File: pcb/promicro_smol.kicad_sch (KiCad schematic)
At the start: 31 parts, among them Q1 HL3134KT, Q2 HL3134KT, Q3 HL3134KT, Q4 HL3134KT, Q5 HL3134KT, U1 LSM6DSVTR, U2 QMC6309, U4 ProMicro NRF52840

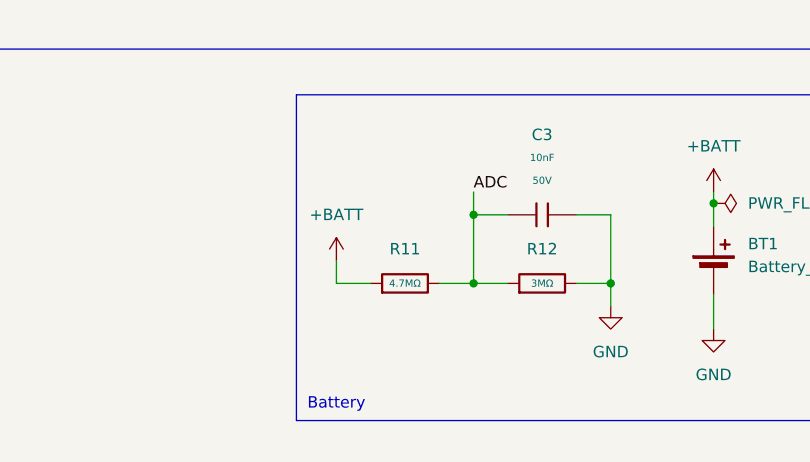
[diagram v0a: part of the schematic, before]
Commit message: feat: routing + ADC res
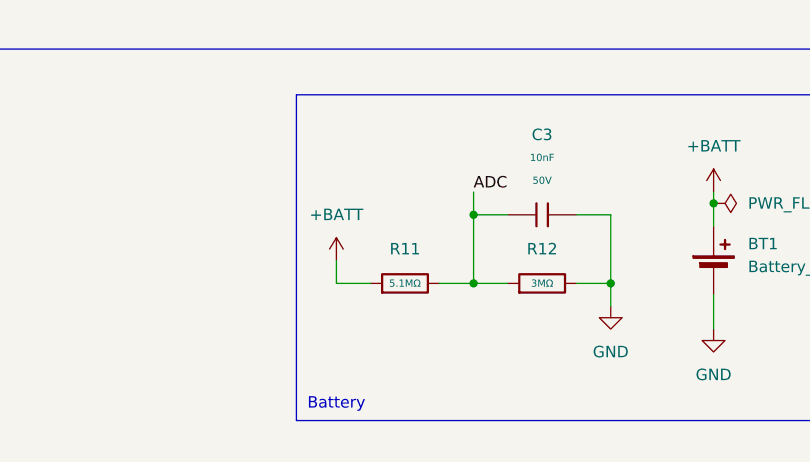
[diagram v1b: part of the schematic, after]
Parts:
- removed R11: 4.7MΩ, PCM_JLCPCB:R_0603, symbol PCM_JLCPCB-Resistors:0603,4.7MΩ
- added R11: 5.1MΩ, PCM_JLCPCB:R_0603, symbol PCM_JLCPCB-Resistors:0603,5.1MΩ
- U4: now left out of the parts list
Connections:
- net +BATT: now also R11.1
- net ADC: now also R11.2
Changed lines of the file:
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@@
 	)
 	(symbol
-		(lib_id "PCM_JLCPCB-Resistors:0603,4.7MΩ")
-		(at 72.39 137.16 90)
-		(unit 1)
-		(exclude_from_sim no)
-		(in_bom yes)
-		(on_board yes)
-		(dnp no)
-		(fields_autoplaced yes)
-		(property "Reference" "R11"
-			(at 72.39 133.35 90)
-			(effects
-				(font
-					(size 1.27 1.27)
-				)
-			)
-		)
-		(property "Value" "4.7MΩ"
-			(at 72.39 137.16 90)
-			(do_not_autoplace yes)
-			(effects
-				(font
-					(size 0.8 0.8)
-				)
-			)
-		)
-		(property "Footprint" "PCM_JLCPCB:R_0603"
-			(at 72.39 138.938 90)
-			(effects
-				(font
-					(size 1.27 1.27)
-				)
-				(hide yes)
-			)
-		)
-		(property "Datasheet" "https://www.lcsc.com/datasheet/lcsc_datasheet_2206010116_UNI-ROYAL-Uniroyal-Elec-0603WAF4704T5E_C23163.pdf"
-			(at 72.39 137.16 0)
-			(effects
-				(font
-					(size 1.27 1.27)
-				)
-				(hide yes)
-			)
-		)
-		(property "Description" "100mW Thick Film Resistors 75V ±100ppm/°C ±1% 4.7MΩ 0603 Chip Resistor - Surface Mount ROHS"
-			(at 72.39 137.16 0)
-			(effects
-				(font
-					(size 1.27 1.27)
-				)
-				(hide yes)
-			)
-		)
-		(property "LCSC" "C23163"
-			(at 72.39 137.16 0)
-			(effects
-				(font
-					(size 1.27 1.27)
-				)
-				(hide yes)
-			)
-		)
-		(property "Stock" "85647"
-			(at 72.39 137.16 0)
-			(effects
-				(font
-					(size 1.27 1.27)
-				)
-				(hide yes)
-			)
-		)
-		(property "Price" "0.005USD"
-			(at 72.39 137.16 0)
-			(effects
-				(font
-					(size 1.27 1.27)
-				)
-				(hide yes)
-			)
-		)
-		(property "Process" "SMT"
-			(at 72.39 137.16 0)
-			(effects
-				(font
-					(size 1.27 1.27)
-				)
-				(hide yes)
-			)
-		)
-		(property "Minimum Qty" "20"
-			(at 72.39 137.16 0)
-			(effects
-				(font
-					(size 1.27 1.27)
-				)
-				(hide yes)
-			)
-		)
-		(property "Attrition Qty" "10"
-			(at 72.39 137.16 0)
-			(effects
-				(font
-					(size 1.27 1.27)
-				)
-				(hide yes)
-			)
-		)
-		(property "Class" "Preferred Component"
-			(at 72.39 137.16 0)
-			(effects
-				(font
-					(size 1.27 1.27)
-				)
-				(hide yes)
-			)
-		)
-		(property "Category" "Resistors,Chip Resistor - Surface Mount"
-			(at 72.39 137.16 0)
-			(effects
-				(font
-					(size 1.27 1.27)
-				)
-				(hide yes)
-			)
-		)
-		(property "Manufacturer" "UNI-ROYAL(Uniroyal Elec)"
-			(at 72.39 137.16 0)
-			(effects
-				(font
-					(size 1.27 1.27)
-				)
-				(hide yes)
-			)
-		)
-		(property "Part" "0603WAF4704T5E"
-			(at 72.39 137.16 0)
-			(effects
-				(font
-					(size 1.27 1.27)
-				)
-				(hide yes)
-			)
-		)
-		(property "Resistance" "4.7MΩ"
-			(at 72.39 137.16 0)
-			(effects
-				(font
-					(size 1.27 1.27)
-				)
-				(hide yes)
-			)
-		)
-		(property "Power(Watts)" "100mW"
-			(at 72.39 137.16 0)
-			(effects
-				(font
-					(size 1.27 1.27)
-				)
-				(hide yes)
-			)
-		)
-		(property "Type" "Thick Film Resistors"
-			(at 72.39 137.16 0)
-			(effects
-				(font
-					(size 1.27 1.27)
-				)
-				(hide yes)
-			)
-		)
-		(property "Overload Voltage (Max)" "75V"
-			(at 72.39 137.16 0)
-			(effects
-				(font
-					(size 1.27 1.27)
-				)
-				(hide yes)
-			)
-		)
-		(property "Operating Temperature Range" "-55°C~+155°C"
-			(at 72.39 137.16 0)
-			(effects
-				(font
-					(size 1.27 1.27)
-				)
-				(hide yes)
-			)
-		)
-		(property "Tolerance" "±1%"
-			(at 72.39 137.16 0)
-			(effects
-				(font
-					(size 1.27 1.27)
-				)
-				(hide yes)
-			)
-		)
-		(property "Temperature Coefficient" "±100ppm/°C"
-			(at 72.39 137.16 0)
-			(effects
-				(font
-					(size 1.27 1.27)
-				)
-				(hide yes)
-			)
-		)
-		(pin "2"
-		)
-		(pin "1"
-		)
-		(instances
-			(project ""
-				(path "/d5cb55fc-68f7-4d45-bbca-416b4e0dde8f"
-					(reference "R11")
-					(unit 1)
-				)
-			)
-		)
-	)
-	(symbol
 		(lib_id "power:GND")
 		(at 123.19 90.17 0)
@@
 	)
 	(symbol
+		(lib_id "PCM_JLCPCB-Resistors:0603,5.1MΩ")
+		(at 72.39 137.16 90)
+		(unit 1)
+		(exclude_from_sim no)
+		(in_bom yes)
+		(on_board yes)
+		(dnp no)
+		(fields_autoplaced yes)
+		(property "Reference" "R11"
+			(at 72.39 133.35 90)
+			(effects
+				(font
+					(size 1.27 1.27)
+				)
+			)
+		)
+		(property "Value" "5.1MΩ"
+			(at 72.39 137.16 90)
+			(do_not_autoplace yes)
+			(effects
+				(font
+					(size 0.8 0.8)
+				)
+			)
+		)
+		(property "Footprint" "PCM_JLCPCB:R_0603"
+			(at 72.39 138.938 90)
+			(effects
+				(font
+					(size 1.27 1.27)
+				)
+				(hide yes)
+			)
+		)
+		(property "Datasheet" "https://www.lcsc.com/datasheet/lcsc_datasheet_2206010216_UNI-ROYAL-Uniroyal-Elec-0603WAF5104T5E_C13320.pdf"
+			(at 72.39 137.16 0)
+			(effects
+				(font
+					(size 1.27 1.27)
+				)
+				(hide yes)
+			)
+		)
+		(property "Description" "100mW Thick Film Resistors 75V ±100ppm/°C ±1% 5.1MΩ 0603 Chip Resistor - Surface Mount ROHS"
+			(at 72.39 137.16 0)
+			(effects
+				(font
+					(size 1.27 1.27)
+				)
+				(hide yes)
+			)
+		)
+		(property "LCSC" "C13320"
+			(at 72.39 137.16 0)
+			(effects
+				(font
+					(size 1.27 1.27)
+				)
+				(hide yes)
+			)
+		)
+		(property "Stock" "196613"
+			(at 72.39 137.16 0)
+			(effects
+				(font
+					(size 1.27 1.27)
+				)
+				(hide yes)
+			)
+		)
+		(property "Price" "0.005USD"
+			(at 72.39 137.16 0)
+			(effects
+				(font
+					(size 1.27 1.27)
+				)
+				(hide yes)
+			)
+		)
+		(property "Process" "SMT"
+			(at 72.39 137.16 0)
+			(effects
+				(font
+					(size 1.27 1.27)
+				)
+				(hide yes)
+			)
+		)
+		(property "Minimum Qty" "20"
+			(at 72.39 137.16 0)
+			(effects
+				(font
+					(size 1.27 1.27)
+				)
+				(hide yes)
+			)
+		)
+		(property "Attrition Qty" "10"
+			(at 72.39 137.16 0)
+			(effects
+				(font
+					(size 1.27 1.27)
+				)
+				(hide yes)
+			)
+		)
+		(property "Class" "Preferred Component"
+			(at 72.39 137.16 0)
+			(effects
+				(font
+					(size 1.27 1.27)
+				)
+				(hide yes)
+			)
+		)
+		(property "Category" "Resistors,Chip Resistor - Surface Mount"
+			(at 72.39 137.16 0)
+			(effects
+				(font
+					(size 1.27 1.27)
+				)
+				(hide yes)
+			)
+		)
+		(property "Manufacturer" "UNI-ROYAL(Uniroyal Elec)"
+			(at 72.39 137.16 0)
+			(effects
+				(font
+					(size 1.27 1.27)
+				)
+				(hide yes)
+			)
+		)
+		(property "Part" "0603WAF5104T5E"
+			(at 72.39 137.16 0)
+			(effects
+				(font
+					(size 1.27 1.27)
+				)
+				(hide yes)
+			)
+		)
+		(property "Resistance" "5.1MΩ"
+			(at 72.39 137.16 0)
+			(effects
+				(font
+					(size 1.27 1.27)
+				)
+				(hide yes)
+			)
+		)
+		(property "Power(Watts)" "100mW"
+			(at 72.39 137.16 0)
+			(effects
+				(font
+					(size 1.27 1.27)
+				)
+				(hide yes)
+			)
+		)
+		(property "Type" "Thick Film Resistors"
+			(at 72.39 137.16 0)
+			(effects
+				(font
+					(size 1.27 1.27)
+				)
+				(hide yes)
+			)
+		)
+		(property "Overload Voltage (Max)" "75V"
+			(at 72.39 137.16 0)
+			(effects
+				(font
+					(size 1.27 1.27)
+				)
+				(hide yes)
+			)
+		)
+		(property "Operating Temperature Range" "-55°C~+155°C"
+			(at 72.39 137.16 0)
+			(effects
+				(font
+					(size 1.27 1.27)
+				)
+				(hide yes)
+			)
+		)
+		(property "Tolerance" "±1%"
+			(at 72.39 137.16 0)
+			(effects
+				(font
+					(size 1.27 1.27)
+				)
+				(hide yes)
+			)
+		)
+		(property "Temperature Coefficient" "±100ppm/°C"
+			(at 72.39 137.16 0)
+			(effects
+				(font
+					(size 1.27 1.27)
+				)
+				(hide yes)
+			)
+		)
+		(pin "1"
+		)
+		(pin "2"
+		)
+		(instances
+			(project ""
+				(path "/d5cb55fc-68f7-4d45-bbca-416b4e0dde8f"
+					(reference "R11")
+					(unit 1)
+				)
+			)
+		)
+	)
+	(symbol
 		(lib_id "PCM_JLCPCB-Resistors:0603,3MΩ")
 		(at 87.63 137.16 90)
@@
 		(unit 1)
 		(exclude_from_sim no)
-		(in_bom yes)
+		(in_bom no)
 		(on_board yes)
 		(dnp no)
